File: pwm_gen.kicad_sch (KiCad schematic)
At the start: 55 parts, among them J2 FAN, J3 STAND, J4 68000-103HLF, Q1 BC847, Q2 2N7002, U1 NE556, U2 NE555D

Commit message: Release 1.0.0
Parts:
- removed D11, D13: LL103A, Diode_SMD:D_MiniMELF, symbol Shottky_diodes:LL103A
- added C25: 1u, Capacitor_SMD:C_0603_1608Metric, symbol CAP_CER_WALSIN_0603:CAP_1u_X7R
- added C9 (x4): 100n, Capacitor_SMD:C_0603_1608Metric, symbol CAP_CER_WALSIN_0603:CAP_100n_X7R
- added Q1 (x2): BC847, Package_TO_SOT_SMD:SOT-23, symbol Transistor_BJT:BC847
- added R12 (x3): 3k3, Resistor_SMD:R_0603_1608Metric, symbol RES_YAGEO_RC0603:RES_3k3_0603
- added R26: 47k, Resistor_SMD:R_0603_1608Metric, symbol RES_YAGEO_RC0603:RES_47k_0603
- added TP4: ~, TestPoint:TestPoint_Pad_D1.0mm, symbol Connector:TestPoint
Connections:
- net +12VA: now also C9.1, C9.1, R12.1; no longer U1.3 (CV)
- net GND: now also C25.2, C9.2, C9.2, C9.2, C9.2, Q1.2 (E), Q1.2 (E)
- net at D15.2 (A2), R6.2, TP4.1: now also RV1.3; no longer RV1.1
- net at D15.2 (A2), R7.1, TP4.1: now also RV1.1; no longer RV1.3
- net at C13.2, Q2.1 (G), R13.1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: now also Q1.3 (C), Q1.3 (C), R12.2
- net at U2.3 (Q): now also R12.2, TP4.1
- net at U2.5 (CV): now also C9.1
- new net: C25.1, Q1.1 (B), R26.2, TP4.1, U2.2 (TR)
- new net: D18.2 (K), D9.1 (K), R12.1, R26.1
- new net: Q1.1 (B), R12.1
- new net: J4.2 (Pin_2), R12.2
- new net: C9.1, U1.3 (CV)
- no-connect marks 2 -> 1
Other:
- moved on the sheet: C1, C13, C14, C2, C3, C7, C8, C9, D1, D13, D15, D18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

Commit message: Release 1.2.0
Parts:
- added R12: 3k3, Resistor_SMD:R_0603_1608Metric, symbol RES_YAGEO_RC0603:RES_3k3_0603
- RV1: footprint Potentiometer:SR_PASSIVES_R16148 -> Koszalix_Poteniometer:SR_PASSIVES_R16148
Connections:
- net at C25.1, R26.2, TP4.1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: now also R12.2; no longer Q1.1 (B)
- new net: Q1.1 (B), R12.1
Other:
- moved on the sheet: Q1, R12, TP4

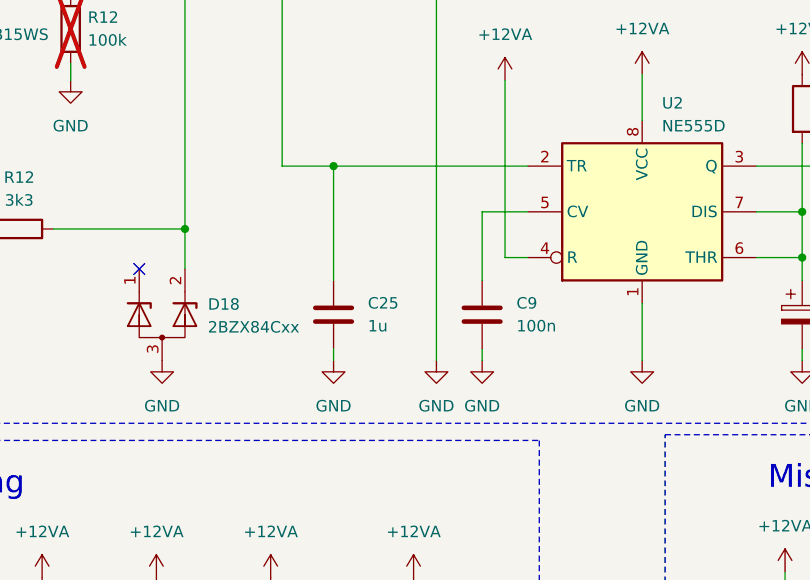
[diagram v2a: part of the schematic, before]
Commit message: Remove C25 from schematic
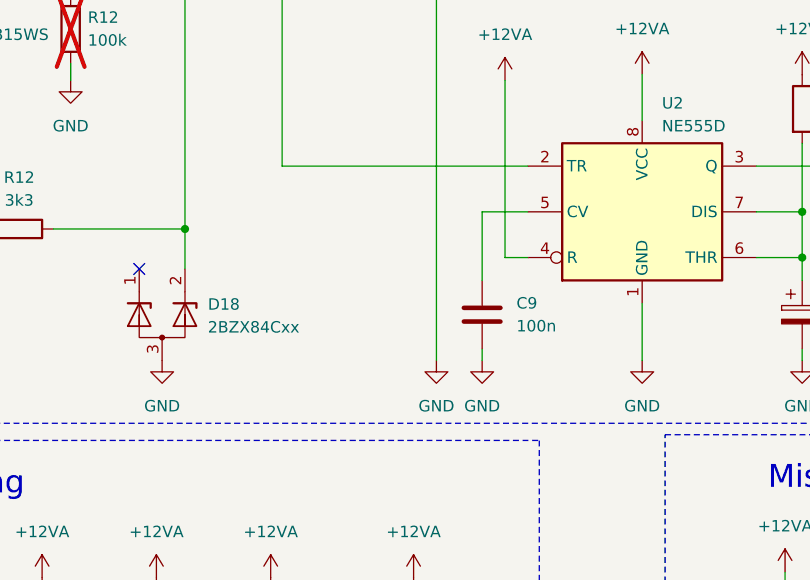
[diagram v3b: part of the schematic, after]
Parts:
- removed C25: 1u, Capacitor_SMD:C_0603_1608Metric, symbol CAP_CER_WALSIN_0603:CAP_1u_X7R
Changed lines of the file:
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@@
   (junction (at 254 106.68) (diameter 0) (color 0 0 0 0)
   )
-  (junction (at 85.09 133.985) (diameter 0) (color 0 0 0 0)
-  )
   (junction (at 68.58 140.97) (diameter 0) (color 0 0 0 0)
   )
@@
     (stroke (width 0) (type default))
   )
-  (wire (pts (xy 85.09 155.575) (xy 85.09 154.305))
-    (stroke (width 0) (type default))
-  )
   (wire (pts (xy 68.58 109.855) (xy 68.58 140.97))
     (stroke (width 0) (type default))
@@
     (stroke (width 0) (type default))
   )
-  (wire (pts (xy 85.09 146.685) (xy 85.09 133.985))
-    (stroke (width 0) (type default))
-  )
   (wire (pts (xy 79.375 133.985) (xy 79.375 109.855))
     (stroke (width 0) (type default))
@@
     (stroke (width 0) (type default))
   )
-  (wire (pts (xy 79.375 133.985) (xy 85.09 133.985))
-    (stroke (width 0) (type default))
-  )
   (wire (pts (xy 96.52 103.505) (xy 106.045 103.505))
     (stroke (width 0) (type default))
@@
     (stroke (width 0) (type default))
   )
-  (wire (pts (xy 85.09 133.985) (xy 106.68 133.985))
+  (wire (pts (xy 79.375 133.985) (xy 106.68 133.985))
     (stroke (width 0) (type default))
   )
@@
     )
   )
-  (symbol (lib_id "CAP_CER_WALSIN_0603:CAP_1u_X7R") (at 85.09 150.495 0) (unit 1)
-    (in_bom yes) (on_board yes) (dnp no) (fields_autoplaced)
-    (property "Reference" "C25" (at 88.9 149.225 0)
-      (effects (font (size 1.27 1.27)) (justify left))
-    )
-    (property "Value" "1u" (at 88.9 151.765 0)
-      (effects (font (size 1.27 1.27)) (justify left))
-    )
-    (property "Footprint" "Capacitor_SMD:C_0603_1608Metric" (at 93.98 146.685 0)
-      (effects (font (size 1.27 1.27)) (justify left) hide)
-    )
-    (property "Datasheet" "https://www.tme.eu/Document/e45476bf270793f696988c4e93ce1237/ASC_General_Purpose.pdf" (at 93.98 149.225 0)
-      (effects (font (size 1.27 1.27)) (justify left) hide)
-    )
-    (property "Manufacturer" "Walsin" (at 93.98 141.605 0)
-      (effects (font (size 1.27 1.27)) (justify left) hide)
-    )
-    (property "MPN" "0603B105K500CT" (at 93.98 144.145 0)
-      (effects (font (size 1.27 1.27)) (justify left) hide)
-    )
-    (property "Tolerance" "10%" (at 93.98 156.845 0)
-      (effects (font (size 1.27 1.27)) (justify left) hide)
-    )
-    (property "Rated voltage" "50V" (at 93.98 154.305 0)
-      (effects (font (size 1.27 1.27)) (justify left) hide)
-    )
-    (property "Operating temperature" "-55°C to +125°C " (at 93.98 151.765 0)
-      (effects (font (size 1.27 1.27)) (justify left) hide)
-    )
-    (property "Capacitance characteristic" "±15%" (at 93.98 159.385 0)
-      (effects (font (size 1.27 1.27)) (justify left) hide)
-    )
-    (pin "1")
-    (pin "2")
-    (instances
-      (project "fumexDriver"
-        (path "/e1f27674-d961-4b58-b2c0-1f4a5bd7ade3/61c0221d-4f1b-4034-b03c-5042ff58f08f"
-          (reference "C25") (unit 1)
-        )
-      )
-    )
-  )
   (symbol (lib_id "power:GND") (at 161.925 73.025 0) (unit 1)
     (in_bom yes) (on_board yes) (dnp no) (fields_autoplaced)
@@
         )
       )
-    )
-  )
-  (symbol (lib_id "power:GND") (at 85.09 155.575 0) (unit 1)
-    (in_bom yes) (on_board yes) (dnp no) (fields_autoplaced)
-    (property "Reference" "#PWR035" (at 85.09 161.925 0)
-      (effects (font (size 1.27 1.27)) hide)
-    )
-    (property "Value" "GND" (at 85.09 160.655 0)
-      (effects (font (size 1.27 1.27)))
-    )
-    (property "Footprint" "" (at 85.09 155.575 0)
-      (effects (font (size 1.27 1.27)) hide)
-    )
-    (property "Datasheet" "" (at 85.09 155.575 0)
-      (effects (font (size 1.27 1.27)) hide)
-    )
-    (pin "1")
-    (instances
-      (project "fumexDriver"
-        (path "/e1f27674-d961-4b58-b2c0-1f4a5bd7ade3"
-          (reference "#PWR035") (unit 1)
-        )
-        (path "/e1f27674-d961-4b58-b2c0-1f4a5bd7ade3/61c0221d-4f1b-4034-b03c-5042ff58f08f"
-          (reference "#PWR096") (unit 1)
-        )
-      )

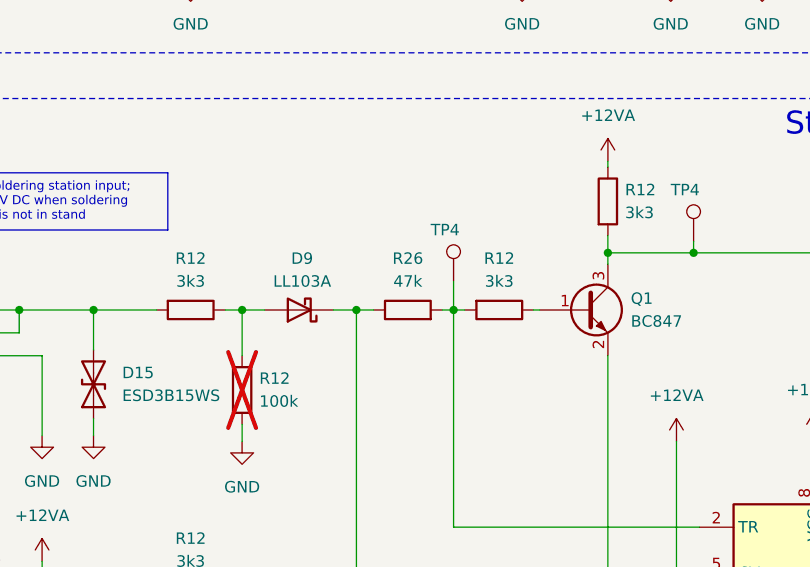
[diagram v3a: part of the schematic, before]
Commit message: Remove R26 from schematic
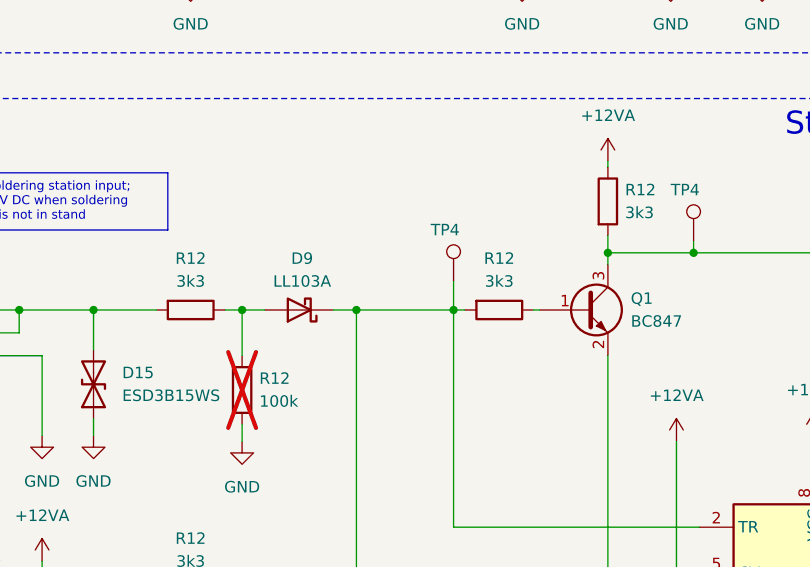
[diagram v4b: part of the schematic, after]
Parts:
- removed R26: 47k, Resistor_SMD:R_0603_1608Metric, symbol RES_YAGEO_RC0603:RES_47k_0603
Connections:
- net at D18.2 (K), D9.1 (K), R12.1: now also R12.2, TP4.1, U2.2 (TR)
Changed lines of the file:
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@@
     (stroke (width 0) (type default))
   )
-  (wire (pts (xy 68.58 109.855) (xy 70.485 109.855))
-    (stroke (width 0) (type default))
-  )
   (wire (pts (xy 65.405 60.325) (xy 86.995 60.325))
     (stroke (width 0) (type default))
@@
     (stroke (width 0) (type default))
   )
-  (wire (pts (xy 79.375 109.855) (xy 78.105 109.855))
+  (wire (pts (xy 68.58 109.855) (xy 79.375 109.855))
     (stroke (width 0) (type default))
   )
@@
         )
       )
-    )
-  )
-  (symbol (lib_id "RES_YAGEO_RC0603:RES_47k_0603") (at 74.295 109.855 90) (unit 1)
-    (in_bom yes) (on_board yes) (dnp no) (fields_autoplaced)
-    (property "Reference" "R26" (at 74.295 104.14 90)
-      (effects (font (size 1.27 1.27)))
-    )
-    (property "Value" "47k" (at 74.295 106.68 90)
-      (effects (font (size 1.27 1.27)))
-    )
-    (property "Footprint" "Resistor_SMD:R_0603_1608Metric" (at 73.025 97.155 0)
-      (effects (font (size 1.27 1.27)) (justify left) hide)
-    )
-    (property "Datasheet" "https://www.tme.eu/Document/d2a72e545e5c8eb7bf2a04fa97535928/rc0603yageo.pdf" (at 73.025 52.705 0)
-      (effects (font (size 1.27 1.27)) (justify left) hide)
-    )
-    (property "Manufacturer" "YAGEO" (at 67.945 97.155 0)
-      (effects (font (size 1.27 1.27)) (justify left) hide)
-    )
-    (property "MPN" "RC0603FR-0747k" (at 70.485 97.155 0)
-      (effects (font (size 1.27 1.27)) (justify left) hide)
-    )
-    (property "Maximum Working Voltage " "50 V" (at 80.645 97.155 0)
-      (effects (font (size 1.27 1.27)) (justify left) hide)
-    )
-    (property "Maximum Overload Voltage" "100 V" (at 85.725 97.155 0)
-      (effects (font (size 1.27 1.27)) (justify left) hide)
-    )
-    (property "Dielectric Withstanding Voltage " "100 V" (at 83.185 97.155 0)
-      (effects (font (size 1.27 1.27)) (justify left) hide)
-    )
-    (property "Temperature Coefficient" "200ppm" (at 78.105 97.155 0)
-      (effects (font (size 1.27 1.27)) (justify left) hide)
-    )
-    (property "Operating Temperature Range" "–55 °C to +155 °C" (at 75.565 97.155 0)
-      (effects (font (size 1.27 1.27)) (justify left) hide)
-    )
-    (property "Tolerance" "1%" (at 78.105 107.315 0)
-      (effects (font (size 1.27 1.27)) (justify left) hide)
-    )
-    (pin "1")
-    (pin "2")
-    (instances
-      (project "fumexDriver"
-        (path "/e1f27674-d961-4b58-b2c0-1f4a5bd7ade3/61c0221d-4f1b-4034-b03c-5042ff58f08f"
-          (reference "R26") (unit 1)
-        )
-      )

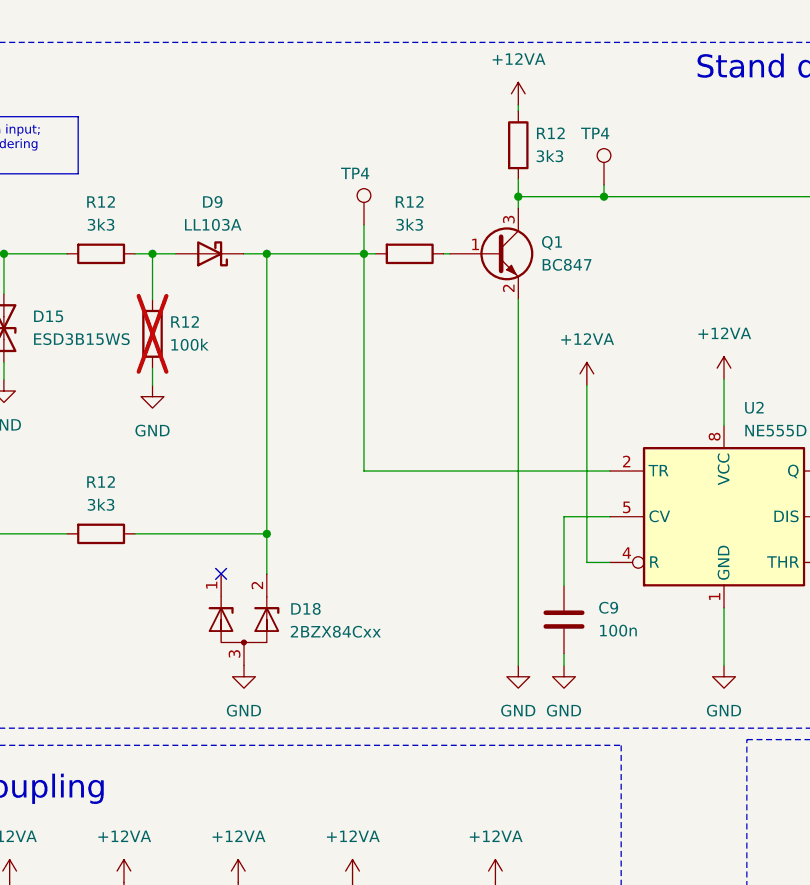
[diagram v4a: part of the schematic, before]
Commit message: Remove D20 from schematic
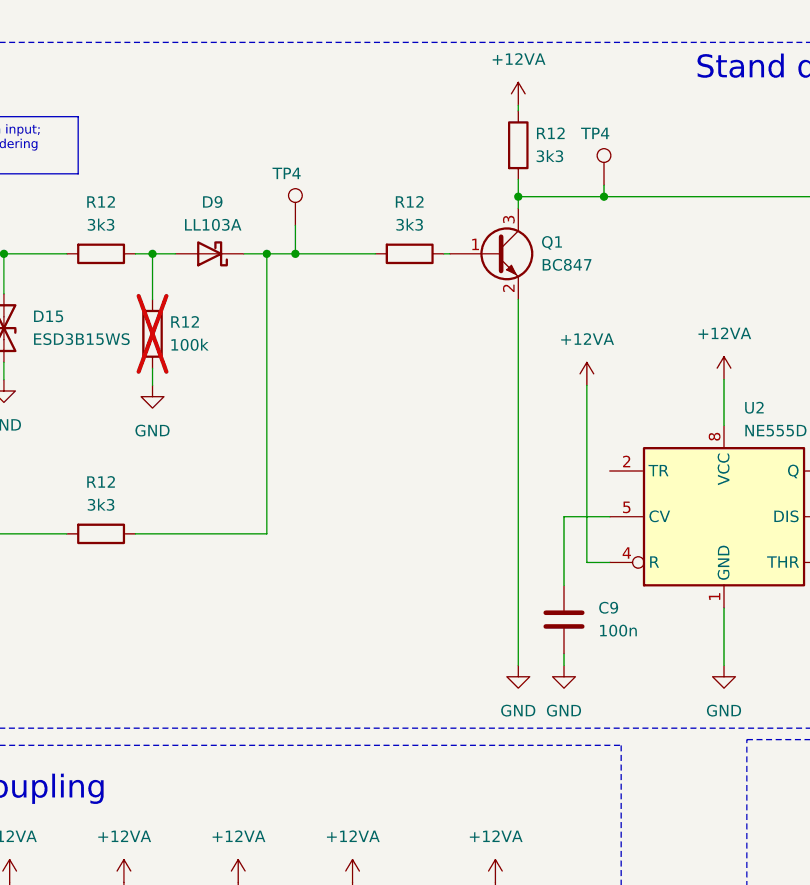
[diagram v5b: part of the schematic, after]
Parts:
- removed D18: 2BZX84Cxx, Package_TO_SOT_SMD:SOT-23, symbol Diode:2BZX84Cxx
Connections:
- net at D9.1 (K), R12.1, R12.2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: no longer U2.2 (TR)
- no-connect marks 1 -> 0
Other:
- moved on the sheet: TP4
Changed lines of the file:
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@@
   (junction (at 254 106.68) (diameter 0) (color 0 0 0 0)
   )
-  (junction (at 68.58 140.97) (diameter 0) (color 0 0 0 0)
-  )
   (junction (at 236.855 101.6) (diameter 0) (color 0 0 0 0)
   )
@@
   (junction (at 186.055 103.505) (diameter 0) (color 0 0 0 0)
   )
+  (junction (at 71.755 109.855) (diameter 0) (color 0 0 0 0)
+  )
   (junction (at 175.895 103.505) (diameter 0) (color 0 0 0 0)
   )
@@
   (junction (at 64.135 26.035) (diameter 0) (color 0 0 0 0)
   )
-  (junction (at 79.375 109.855) (diameter 0) (color 0 0 0 0)
-  )
   (junction (at 135.255 190.5) (diameter 0) (color 0 0 0 0)
   )
@@
   (junction (at 236.855 47.625) (diameter 0) (color 0 0 0 0)
   )
-  (no_connect (at 63.5 145.415))
   (wire (pts (xy 233.045 47.625) (xy 236.855 47.625))
     (stroke (width 0) (type default))
@@
     (stroke (width 0) (type default))
   )
-  (wire (pts (xy 68.58 140.97) (xy 68.58 145.415))
-    (stroke (width 0) (type default))
-  )
   (wire (pts (xy 146.05 133.985) (xy 147.955 133.985))
     (stroke (width 0) (type default))
@@
     (stroke (width 0) (type default))
   )
-  (wire (pts (xy 79.375 109.855) (xy 80.645 109.855))
-    (stroke (width 0) (type default))
-  )
   (wire (pts (xy 132.08 133.985) (xy 146.05 133.985))
     (stroke (width 0) (type default))
@@
     (stroke (width 0) (type default))
   )
-  (wire (pts (xy 79.375 133.985) (xy 79.375 109.855))
-    (stroke (width 0) (type default))
-  )
   (wire (pts (xy 53.975 109.855) (xy 55.88 109.855))
     (stroke (width 0) (type default))
@@
     (stroke (width 0) (type default))
   )
-  (wire (pts (xy 79.375 133.985) (xy 106.68 133.985))
-    (stroke (width 0) (type default))
-  )
   (wire (pts (xy 86.995 73.025) (xy 86.995 70.485))
     (stroke (width 0) (type default))
@@
     (stroke (width 0) (type default))
   )
+  (wire (pts (xy 71.755 109.855) (xy 80.645 109.855))
+    (stroke (width 0) (type default))
+  )
   (wire (pts (xy 196.215 73.66) (xy 196.215 62.865))
     (stroke (width 0) (type default))
@@
     (stroke (width 0) (type default))
   )
-  (wire (pts (xy 68.58 109.855) (xy 79.375 109.855))
+  (wire (pts (xy 68.58 109.855) (xy 71.755 109.855))
     (stroke (width 0) (type default))
   )
@@
     (stroke (width 0) (type default))
   )
-  (wire (pts (xy 79.375 106.68) (xy 79.375 109.855))
+  (wire (pts (xy 71.755 106.68) (xy 71.755 109.855))
     (stroke (width 0) (type default))
   )
@@
     )
   )
-  (symbol (lib_id "Diode:2BZX84Cxx") (at 66.04 150.495 0) (unit 1)
-    (in_bom yes) (on_board yes) (dnp no) (fields_autoplaced)
-    (property "Reference" "D18" (at 71.12 149.352 0)
-      (effects (font (size 1.27 1.27)) (justify left))
-    )
-    (property "Value" "2BZX84Cxx" (at 71.12 151.892 0)
-      (effects (font (size 1.27 1.27)) (justify left))
-    )
-    (property "Footprint" "Package_TO_SOT_SMD:SOT-23" (at 69.85 153.035 0)
-      (effects (font (size 1.27 1.27)) (justify left) hide)
-    )
-    (property "Datasheet" "https://diotec.com/tl_files/diotec/files/pdf/datasheets/bzx84c2v4.pdf" (at 63.5 150.495 90)
-      (effects (font (size 1.27 1.27)) hide)
-    )
-    (pin "1")
-    (pin "2")
-    (pin "3")
-    (instances
-      (project "fumexDriver"
-        (path "/e1f27674-d961-4b58-b2c0-1f4a5bd7ade3/dbd0426a-8822-4787-8e38-b43529a352bf"
-          (reference "D18") (unit 1)
-        )
-        (path "/e1f27674-d961-4b58-b2c0-1f4a5bd7ade3/61c0221d-4f1b-4034-b03c-5042ff58f08f"
-          (reference "D20") (unit 1)
-        )
-      )
-    )
-  )
   (symbol (lib_id "Connector:TestPoint") (at 196.215 36.83 0) (unit 1)
     (in_bom yes) (on_board yes) (dnp no)
@@
     )
   )
-  (symbol (lib_id "Connector:TestPoint") (at 79.375 106.68 0) (unit 1)
+  (symbol (lib_id "Connector:TestPoint") (at 71.755 106.68 0) (unit 1)
     (in_bom yes) (on_board yes) (dnp no)
-    (property "Reference" "TP4" (at 76.835 100.965 0)
+    (property "Reference" "TP4" (at 69.215 100.965 0)
       (effects (font (size 1.27 1.27)) (justify left))
     )
-    (property "Value" "~" (at 76.835 100.33 0)
+    (property "Value" "~" (at 69.215 100.33 0)
       (effects (font (size 1.27 1.27)) (justify left) hide)
     )
-    (property "Footprint" "TestPoint:TestPoint_Pad_D1.0mm" (at 84.455 106.68 0)
+    (property "Footprint" "TestPoint:TestPoint_Pad_D1.0mm" (at 76.835 106.68 0)
       (effects (font (size 1.27 1.27)) hide)
     )
-    (property "Datasheet" "~" (at 84.455 106.68 0)
+    (property "Datasheet" "~" (at 76.835 106.68 0)
       (effects (font (size 1.27 1.27)) hide)
     )
@@
         )
       )
-    )
-  )
-  (symbol (lib_id "power:GND") (at 66.04 155.575 0) (unit 1)
-    (in_bom yes) (on_board yes) (dnp no) (fields_autoplaced)
-    (property "Reference" "#PWR035" (at 66.04 161.925 0)
-      (effects (font (size 1.27 1.27)) hide)
-    )
-    (property "Value" "GND" (at 66.04 160.655 0)
-      (effects (font (size 1.27 1.27)))
-    )
-    (property "Footprint" "" (at 66.04 155.575 0)
-      (effects (font (size 1.27 1.27)) hide)
-    )
-    (property "Datasheet" "" (at 66.04 155.575 0)
-      (effects (font (size 1.27 1.27)) hide)
-    )
-    (pin "1")
-    (instances
-      (project "fumexDriver"
-        (path "/e1f27674-d961-4b58-b2c0-1f4a5bd7ade3"
-          (reference "#PWR035") (unit 1)
-        )
-        (path "/e1f27674-d961-4b58-b2c0-1f4a5bd7ade3/61c0221d-4f1b-4034-b03c-5042ff58f08f"
-          (reference "#PWR084") (unit 1)
-        )
-      )
